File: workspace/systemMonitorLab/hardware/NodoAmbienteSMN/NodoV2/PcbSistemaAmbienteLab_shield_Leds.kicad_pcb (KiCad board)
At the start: 2 copper layers, 14.5 x 21.2 mm, 3 parts, among them J7 Molex_Led_Status

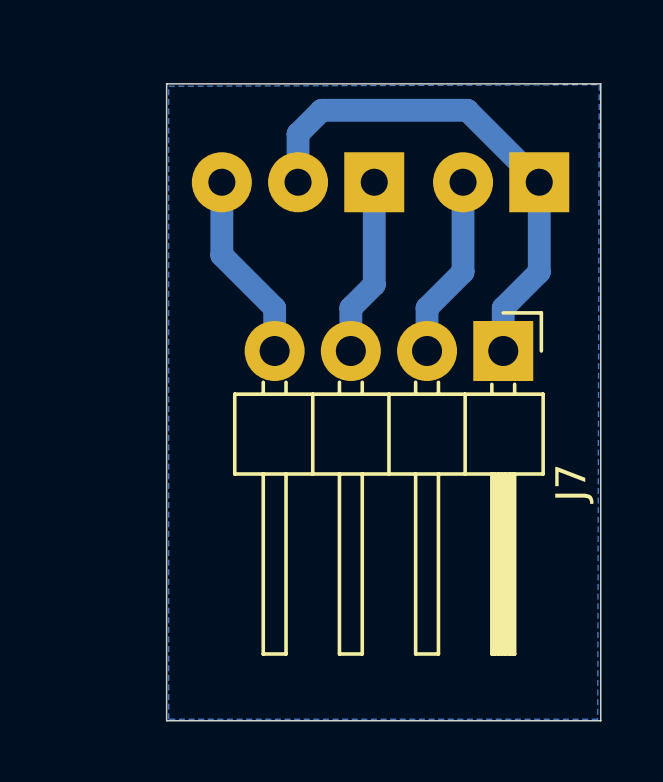
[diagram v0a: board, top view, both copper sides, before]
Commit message: Subo el resideño de los pcb's acorde al case 3d
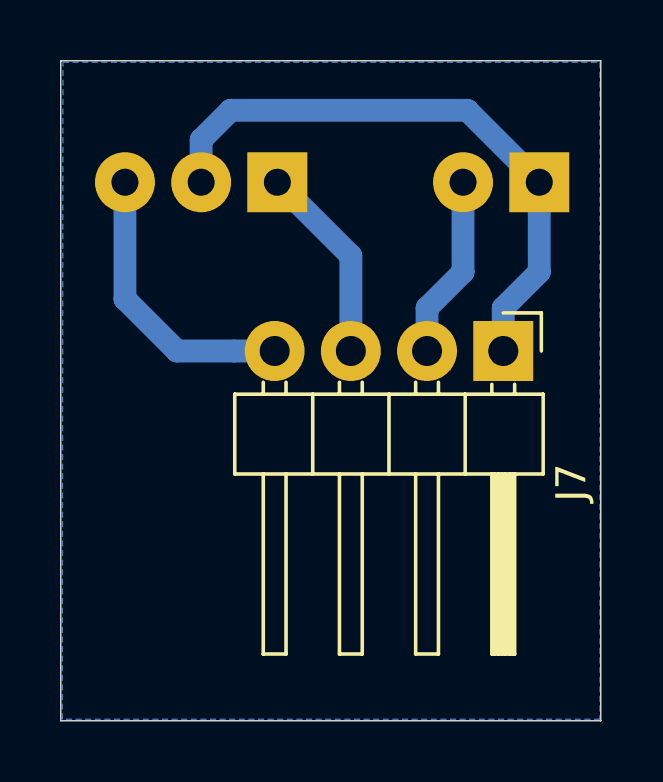
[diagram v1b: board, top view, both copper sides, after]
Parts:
- moved D2 3.23 mm to (164.3, 81.0)
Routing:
- net Net-(D2-A2): track 6.35 -> 11.6 mm
- net GND: track 17.1 -> 22.0 mm
- net Net-(D2-A1): track 5.95 -> 6.64 mm
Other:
- board size 14.5 x 21.2 mm -> 18 x 22 mm
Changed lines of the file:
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@@
 	(footprint "LED_THT:LED_D3.0mm-3"
 		(layer "B.Cu")
-		(at 167.5 81 180)
+		(at 164.27 81 180)
 		(descr "LED, diameter 3.0mm, 3 pins, https://www.kingbright.com/attachments/file/psearch/000/00/00/L-3VSURKCGKC(Ver.12A).pdf, generated by kicad-footprint-generator")
 		(tags "LED")
@@
 	)
 	(gr_rect
-		(start 160.58 77.72)
+		(start 157.05 76.95)
 		(end 175.05 98.95)
 		(stroke
@@
 		(layer "Dwgs.User")
 		(pts
-			(xy 160.58 98.95) (xy 175.05 98.95)
-		)
-		(height 3.55)
+			(xy 175.05 76.95) (xy 175.05 98.95)
+		)
+		(height 2.875)
+		(orientation 1)
+		(format
+			(prefix "")
+			(suffix "")
+			(units 3)
+			(units_format 0)
+			(precision 4)
+			(suppress_zeroes yes)
+		)
+		(style
+			(thickness 0.1)
+			(arrow_length 1.27)
+			(text_position_mode 0)
+			(arrow_direction outward)
+			(extension_height 0.58642)
+			(extension_offset 0.5)
+			(keep_text_aligned yes)
+		)
+		(gr_text "22"
+			(at 176.775 87.95 90)
+			(layer "Dwgs.User")
+			(effects
+				(font
+					(size 1 1)
+					(thickness 0.15)
+				)
+			)
+		)
+	)
+	(dimension
+		(type orthogonal)
+		(layer "Dwgs.User")
+		(pts
+			(xy 161.725 81) (xy 161.75 76.95)
+		)
+		(height -11.825)
+		(orientation 1)
+		(format
+			(prefix "")
+			(suffix "")
+			(units 3)
+			(units_format 0)
+			(precision 4)
+			(suppress_zeroes yes)
+		)
+		(style
+			(thickness 0.1)
+			(arrow_length 1.27)
+			(text_position_mode 0)
+			(arrow_direction outward)
+			(extension_height 0.58642)
+			(extension_offset 0.5)
+			(keep_text_aligned yes)
+		)
+		(gr_text "4.05"
+			(at 148.75 78.975 90)
+			(layer "Dwgs.User")
+			(effects
+				(font
+					(size 1 1)
+					(thickness 0.15)
+				)
+			)
+		)
+	)
+	(dimension
+		(type orthogonal)
+		(layer "Dwgs.User")
+		(pts
+			(xy 157.05 98.95) (xy 175.05 98.95)
+		)
+		(height 2.525)
 		(orientation 0)
 		(format
@@
 			(keep_text_aligned yes)
 		)
-		(gr_text "14.47"
-			(at 167.815 101.35 0)
+		(gr_text "18"
+			(at 166.05 100.325 0)
 			(layer "Dwgs.User")
 			(effects
@@
 		(layer "Dwgs.User")
 		(pts
-			(xy 175.05 77.72) (xy 175.05 98.95)
-		)
-		(height 3.9)
+			(xy 161.73 81) (xy 171.73 81)
+		)
+		(height -9.05)
+		(orientation 0)
+		(format
+			(prefix "")
+			(suffix "")
+			(units 3)
+			(units_format 0)
+			(precision 4)
+			(suppress_zeroes yes)
+		)
+		(style
+			(thickness 0.1)
+			(arrow_length 1.27)
+			(text_position_mode 0)
+			(arrow_direction outward)
+			(extension_height 0.58642)
+			(extension_offset 0.5)
+			(keep_text_aligned yes)
+		)
+		(gr_text "10"
+			(at 166.73 70.8 0)
+			(layer "Dwgs.User")
+			(effects
+				(font
+					(size 1 1)
+					(thickness 0.15)
+				)
+			)
+		)
+	)
+	(dimension
+		(type orthogonal)
+		(layer "Dwgs.User")
+		(pts
+			(xy 161.73 81) (xy 161.7 98.925)
+		)
+		(height -11.855)
 		(orientation 1)
 		(format
@@
 			(keep_text_aligned yes)
 		)
-		(gr_text "21.23"
-			(at 177.8 88.335 90)
+		(gr_text "17.925"
+			(at 148.725 89.9625 90)
 			(layer "Dwgs.User")
 			(effects
@@
 	)
 	(segment
-		(start 164.96 81)
-		(end 164.96 79.39)
-		(width 0.762)
-		(layer "B.Cu")
-		(net 1)
-	)
-	(segment
-		(start 165.748 78.602)
+		(start 161.73 79.585787)
+		(end 161.73 81)
+		(width 0.762)
+		(layer "B.Cu")
+		(net 1)
+	)
+	(segment
+		(start 162.713787 78.602)
+		(end 161.73 79.585787)
+		(width 0.762)
+		(layer "B.Cu")
+		(net 1)
+	)
+	(segment
+		(start 173 81)
 		(end 170.602 78.602)
-		(width 0.762)
-		(layer "B.Cu")
-		(net 1)
-	)
-	(segment
-		(start 170.602 78.602)
-		(end 173 81)
 		(width 0.762)
 		(layer "B.Cu")
@@
 	)
 	(segment
+		(start 170.602 78.602)
+		(end 162.713787 78.602)
+		(width 0.762)
+		(layer "B.Cu")
+		(net 1)
+	)
+	(segment
 		(start 171.8 86.625)
 		(end 171.8 85.1923)
@@
 	)
 	(segment
-		(start 164.96 79.39)
-		(end 165.748 78.602)
-		(width 0.762)
-		(layer "B.Cu")
-		(net 1)
+		(start 161.73 81)
+		(end 161.73 79.195)
+		(width 0.2)
+		(layer "B.Cu")
+		(net 1)
+	)
+	(segment
+		(start 160.925 86.625)
+		(end 162.825 86.625)
+		(width 0.762)
+		(layer "B.Cu")
+		(net 2)
 	)
 	(segment
 		(start 164.18 86.625)
-		(end 164.18 85.1923)
-		(width 0.762)
-		(layer "B.Cu")
-		(net 2)
-	)
-	(segment
-		(start 162.42 83.4323)
-		(end 164.18 85.1923)
-		(width 0.762)
-		(layer "B.Cu")
-		(net 2)
-	)
-	(segment
-		(start 162.42 81)
-		(end 162.42 83.4323)
-		(width 0.762)
-		(layer "B.Cu")
-		(net 2)
-	)
-	(segment
-		(start 167.5 81)
-		(end 167.5 84.4123)
+		(end 162.825 86.625)
+		(width 0.762)
+		(layer "B.Cu")
+		(net 2)
+	)
+	(segment
+		(start 159.19 84.89)
+		(end 159.19 81)
+		(width 0.762)
+		(layer "B.Cu")
+		(net 2)
+	)
+	(segment
+		(start 159.19 84.89)
+		(end 160.925 86.625)
+		(width 0.762)
+		(layer "B.Cu")
+		(net 2)
+	)
+	(segment
+		(start 159.19 81.385)
+		(end 159.075 81.5)
+		(width 0.2)
+		(layer "B.Cu")
+		(net 2)
+	)
+	(segment
+		(start 159.19 81)
+		(end 159.19 81.385)
+		(width 0.2)
+		(layer "B.Cu")
+		(net 2)
+	)
+	(segment
+		(start 162.825 86.625)
+		(end 161.325 86.625)
+		(width 0.2)
+		(layer "B.Cu")
+		(net 2)
+	)
+	(segment
+		(start 166.72 83.45)
+		(end 164.27 81)
 		(width 0.762)
 		(layer "B.Cu")
@@
 	)
 	(segment
-		(start 167.5 84.4123)
-		(end 166.72 85.1923)
-		(width 0.762)
-		(layer "B.Cu")
-		(net 3)
-	)
-	(segment
 		(start 166.72 86.625)
-		(end 166.72 85.1923)
+		(end 166.72 83.45)
 		(width 0.762)
 		(layer "B.Cu")
@@
 		(polygon
 			(pts
-				(xy 160.65 77.8) (xy 175 77.75) (xy 174.95 98.9) (xy 160.65 98.9)
-			)
-		)
+				(xy 157.125 77) (xy 175.025 77) (xy 175.025 98.9) (xy 157.1 98.9)
+			)
+		)

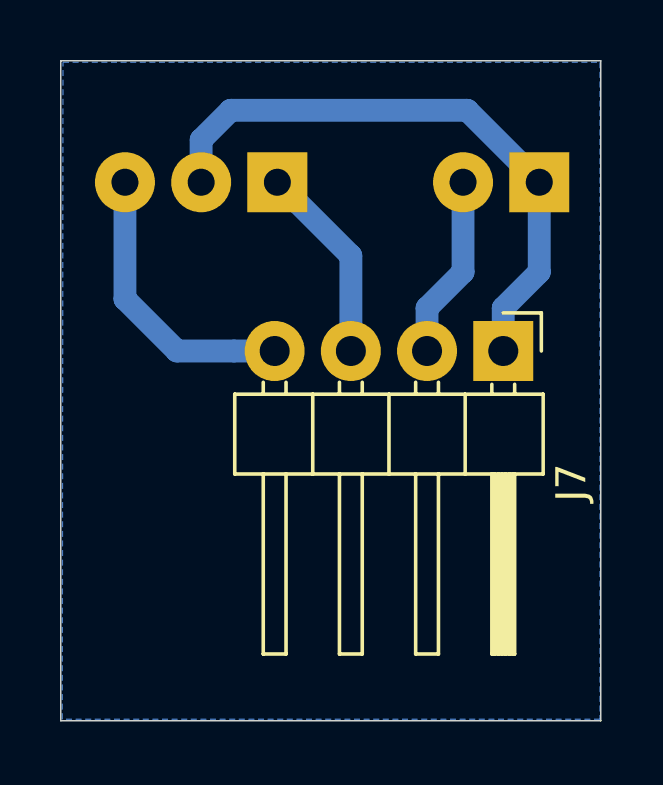
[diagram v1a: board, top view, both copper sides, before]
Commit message: Tareas Realizadas: 	- Se corrije la disposicion de los conectores, para que el cable 	  quede derecho en su construccion se tiene que invertir el 	  orden de los pines en las placas led_status y sensors. 	- Se Cambio el ancho de las pistas que atraviesan a los 	  resistores SMD de 30 a 25 mils. 	- Se esta transmitiendo al sevirdor nginx por el puerto 80. Tareas proximas: 	- Se debe Contruir las placas y realizar pruebas. 	- Modificar el firmware para que los led envien los estados por 	  PWM para el LED dual. y On - OFF para el Led simple. 	- Se debe agregar un filtro para que los datos que tengan una 	  varianza mayor a un valor x no se transmitan. 	- Se debe agregar un retardo para que no se transmitan los datos 	  de inicio del barometro, ya que siempre marcan un valor 	  alredeor de 700 hPa.
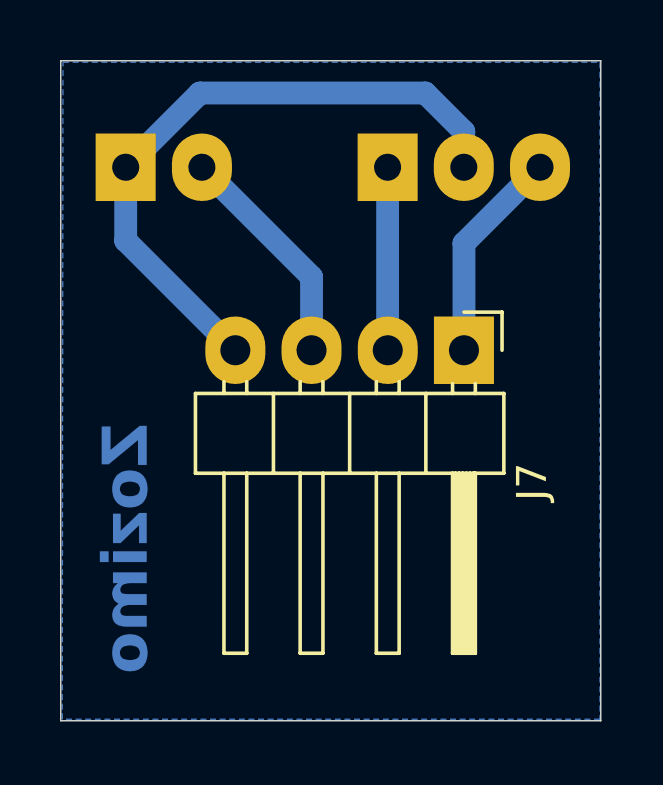
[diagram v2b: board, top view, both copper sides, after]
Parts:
- moved D1 13.8 mm to (159.2, 80.5), turned to 0 degrees
- moved D2 3.71 mm to (167.9, 80.5), turned to 0 degrees
- moved J7 1.31 mm to (170.5, 86.6)
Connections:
- J7 pad 1: GND -> Net-(D2-A2)
- J7 pad 2: Net-(D1-A) -> Net-(D2-A1)
- J7 pad 3: Net-(D2-A1) -> Net-(D1-A)
- J7 pad 4: Net-(D2-A2) -> GND
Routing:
- net Net-(D2-A2): track 11.6 -> 7.15 mm
- net Net-(D1-A): track 6.12 -> 7.61 mm
- net GND: track 22.0 -> 23.1 mm
- net Net-(D2-A1): track 6.64 -> 6.10 mm
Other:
- board text added: "Zozimo"

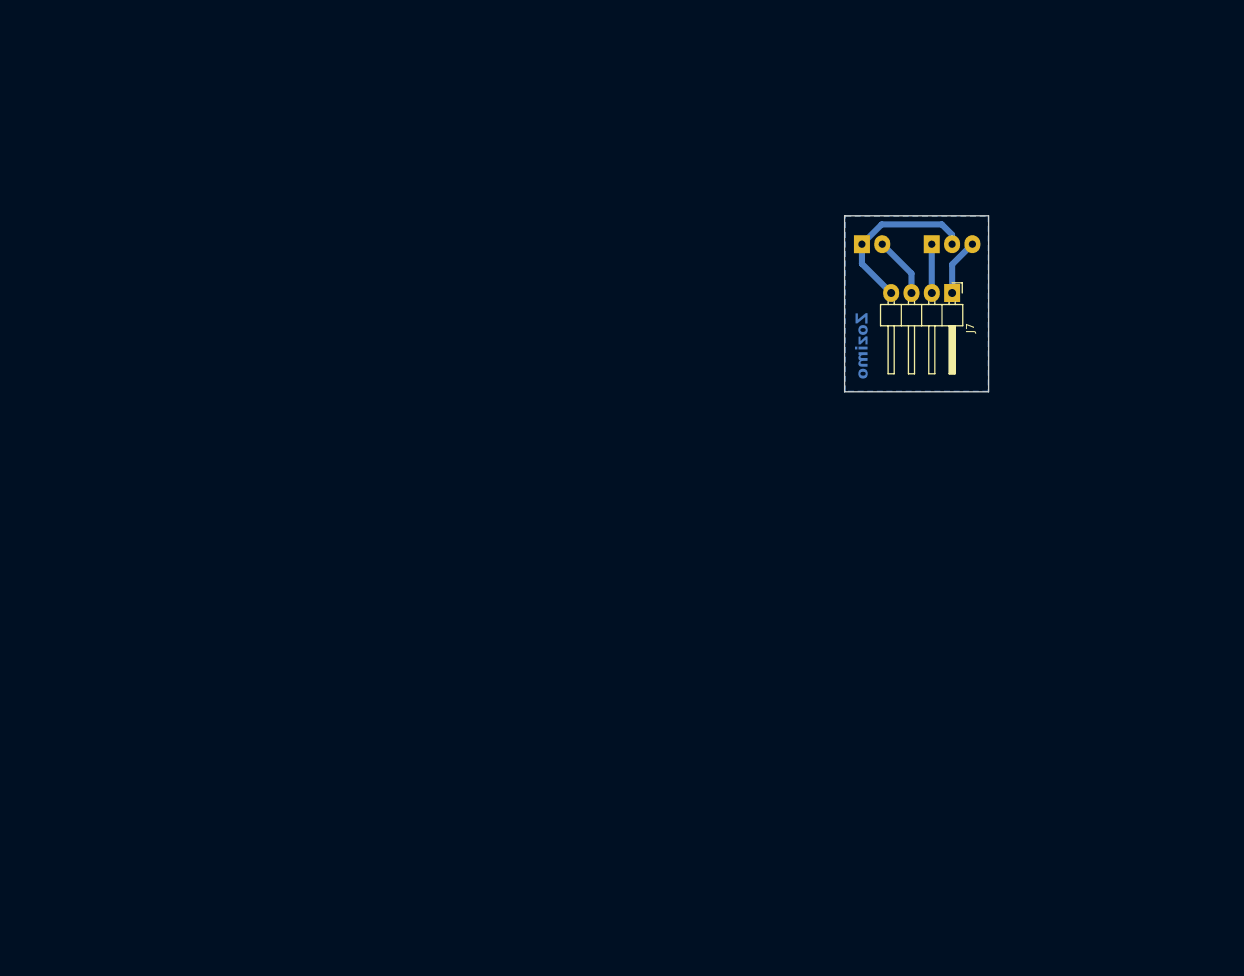
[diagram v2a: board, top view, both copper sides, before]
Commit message: Se mejora el plano de masa del PCB
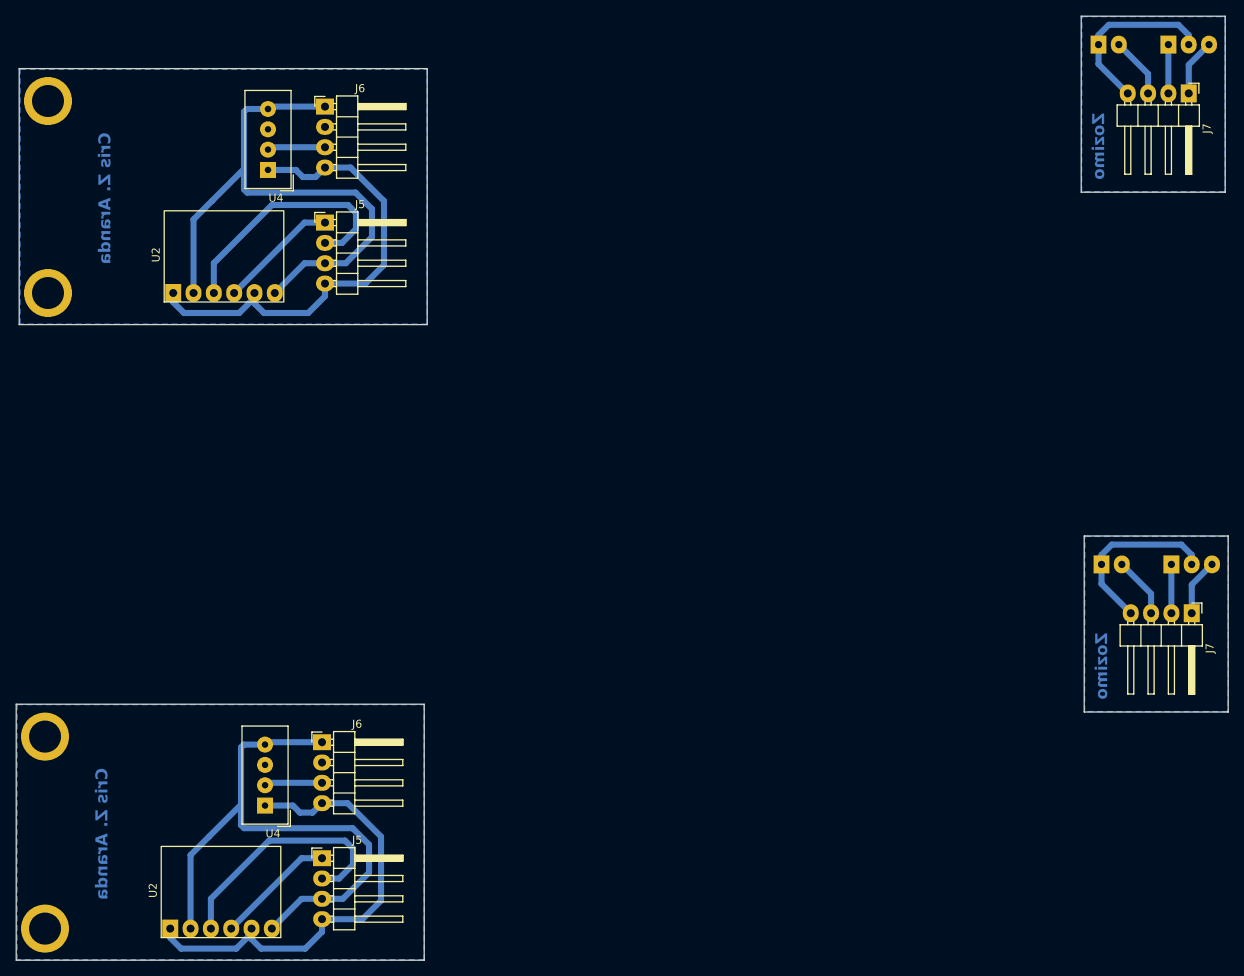
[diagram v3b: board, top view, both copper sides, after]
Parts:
- added ?: , , F.Cu at (57.5, 86.6)
- added ?: , , F.Cu at (57.5, 62.6)
- added ?: , , F.Cu at (57.1, 166.1)
- added ?: , , F.Cu at (57.1, 142.1)
- added D1: LED_YELLOW, LED_THT:LED_D3.0mm, B.Cu at (189.2, 120.5)
- added D2: LED_Dual_AKA, LED_THT:LED_D3.0mm-3, B.Cu at (197.9, 120.5)
- added J5: Molex_Sensor_BMP280, Connector_PinHeader_2.54mm:PinHeader_1x04_P2.54mm_Horizontal, F.Cu at (92.1, 77.8)
- added J5: Molex_Sensor_BMP280, Connector_PinHeader_2.54mm:PinHeader_1x04_P2.54mm_Horizontal, F.Cu at (91.7, 157.2)
- added J6: Molex_Sensor_DHT22, Connector_PinHeader_2.54mm:PinHeader_1x04_P2.54mm_Horizontal, F.Cu at (91.7, 142.8)
- added J6: Molex_Sensor_DHT22, Connector_PinHeader_2.54mm:PinHeader_1x04_P2.54mm_Horizontal, F.Cu at (92.1, 63.3)
- added J7: Molex_Led_Status, Connector_PinHeader_2.54mm:PinHeader_1x04_P2.54mm_Horizontal, F.Cu at (200.4, 126.6)
- added U2: Bmp280Module, Modulos_comerciales:BMP280_Module, F.Cu at (72.8, 166.1)
- added U2: Bmp280Module, Modulos_comerciales:BMP280_Module, F.Cu at (73.1, 86.6)
- added U4: DHT22, Sensor:Aosong_DHT11_5.5x12.0_P2.54mm, F.Cu at (84.6, 150.7)
- added U4: DHT22, Sensor:Aosong_DHT11_5.5x12.0_P2.54mm, F.Cu at (85.0, 71.2)
- moved D2 38.7 mm to (197.5, 55.5)
- moved D1 38.7 mm to (188.8, 55.5)
- moved J7 38.7 mm to (200.1, 61.6)
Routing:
- net GND: track 23.1 -> 195.2 mm
- net 3V3: track 0.00 -> 119.5 mm
- net Net-(J5-Pin_2): track 0.00 -> 63.0 mm
- net Net-(J5-Pin_1): track 0.00 -> 30.0 mm
- net Net-(J6-Pin_3): track 0.00 -> 14.5 mm
- net Net-(D1-A): track 7.61 -> 15.2 mm
- net Net-(D2-A2): track 7.15 -> 14.3 mm
- net Net-(D2-A1): track 6.10 -> 12.2 mm
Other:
- board size 18 x 22 mm -> 151.5 x 118 mm
- board text added: "Cris Z. Aranda"
